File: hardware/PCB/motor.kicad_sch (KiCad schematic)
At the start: 32 parts, among them J1 Turntable Stepper, J2 Gantry Stepper, J3 Extruder Stepper, J4 Revolute Stepper

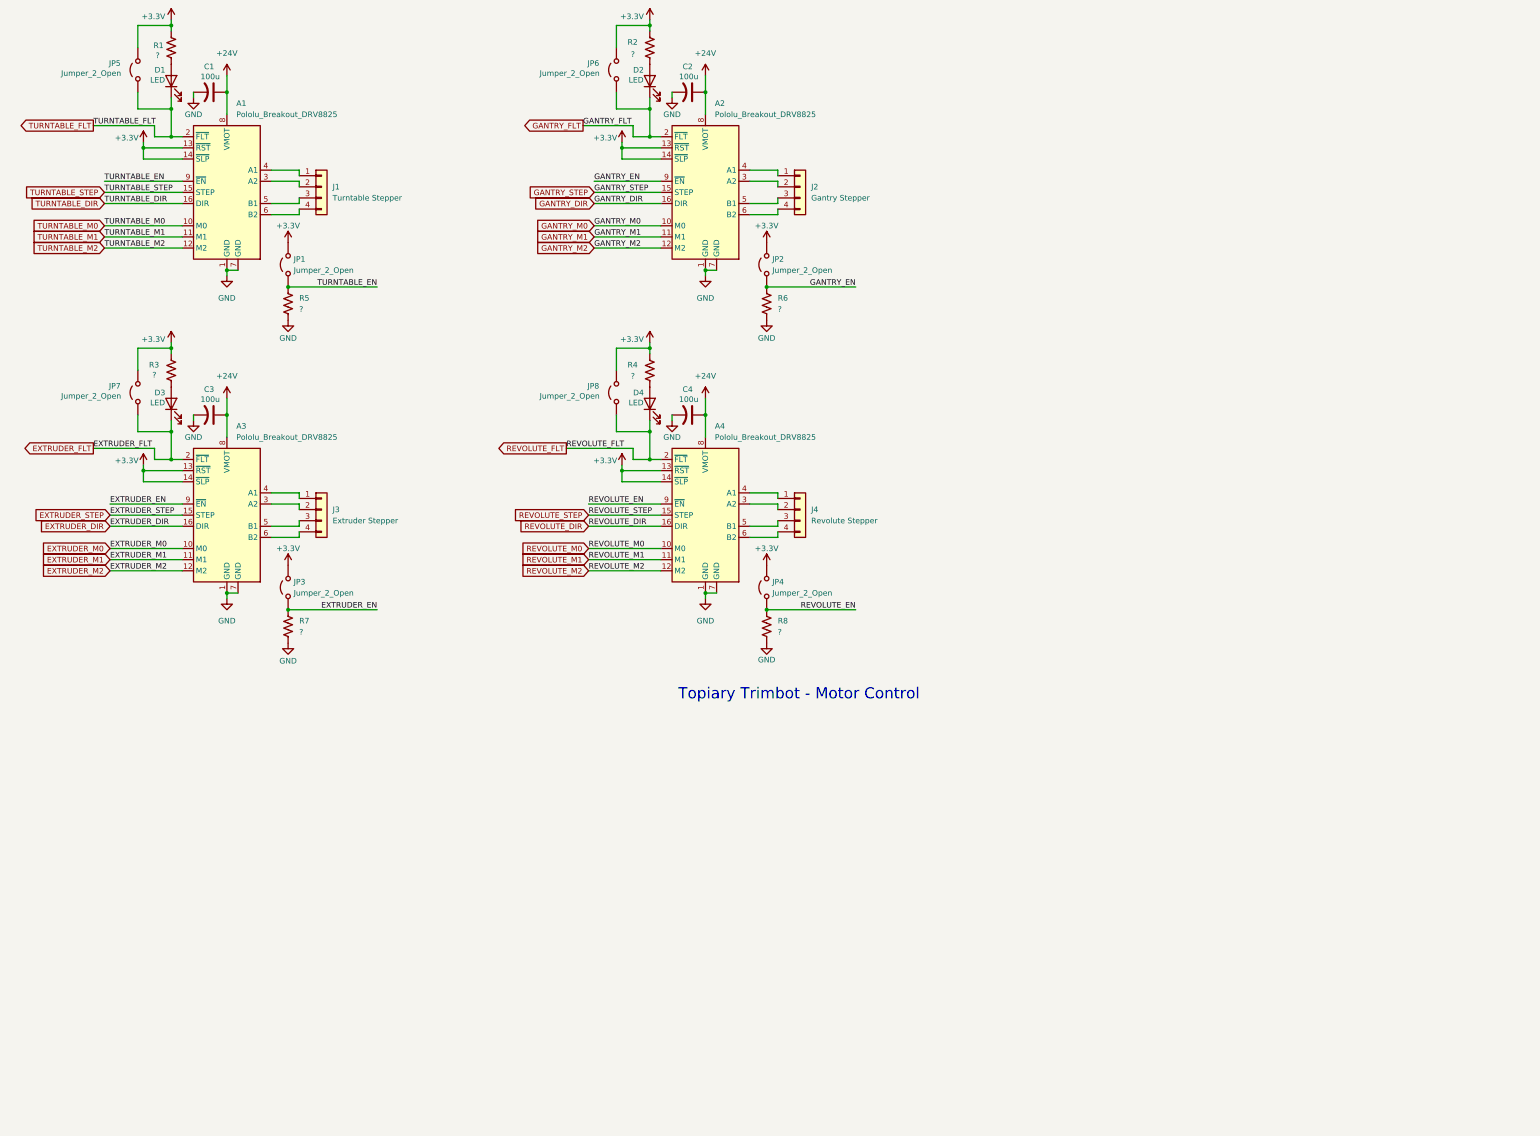
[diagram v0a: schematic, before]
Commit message: Schematic - Microstepping Jumpers
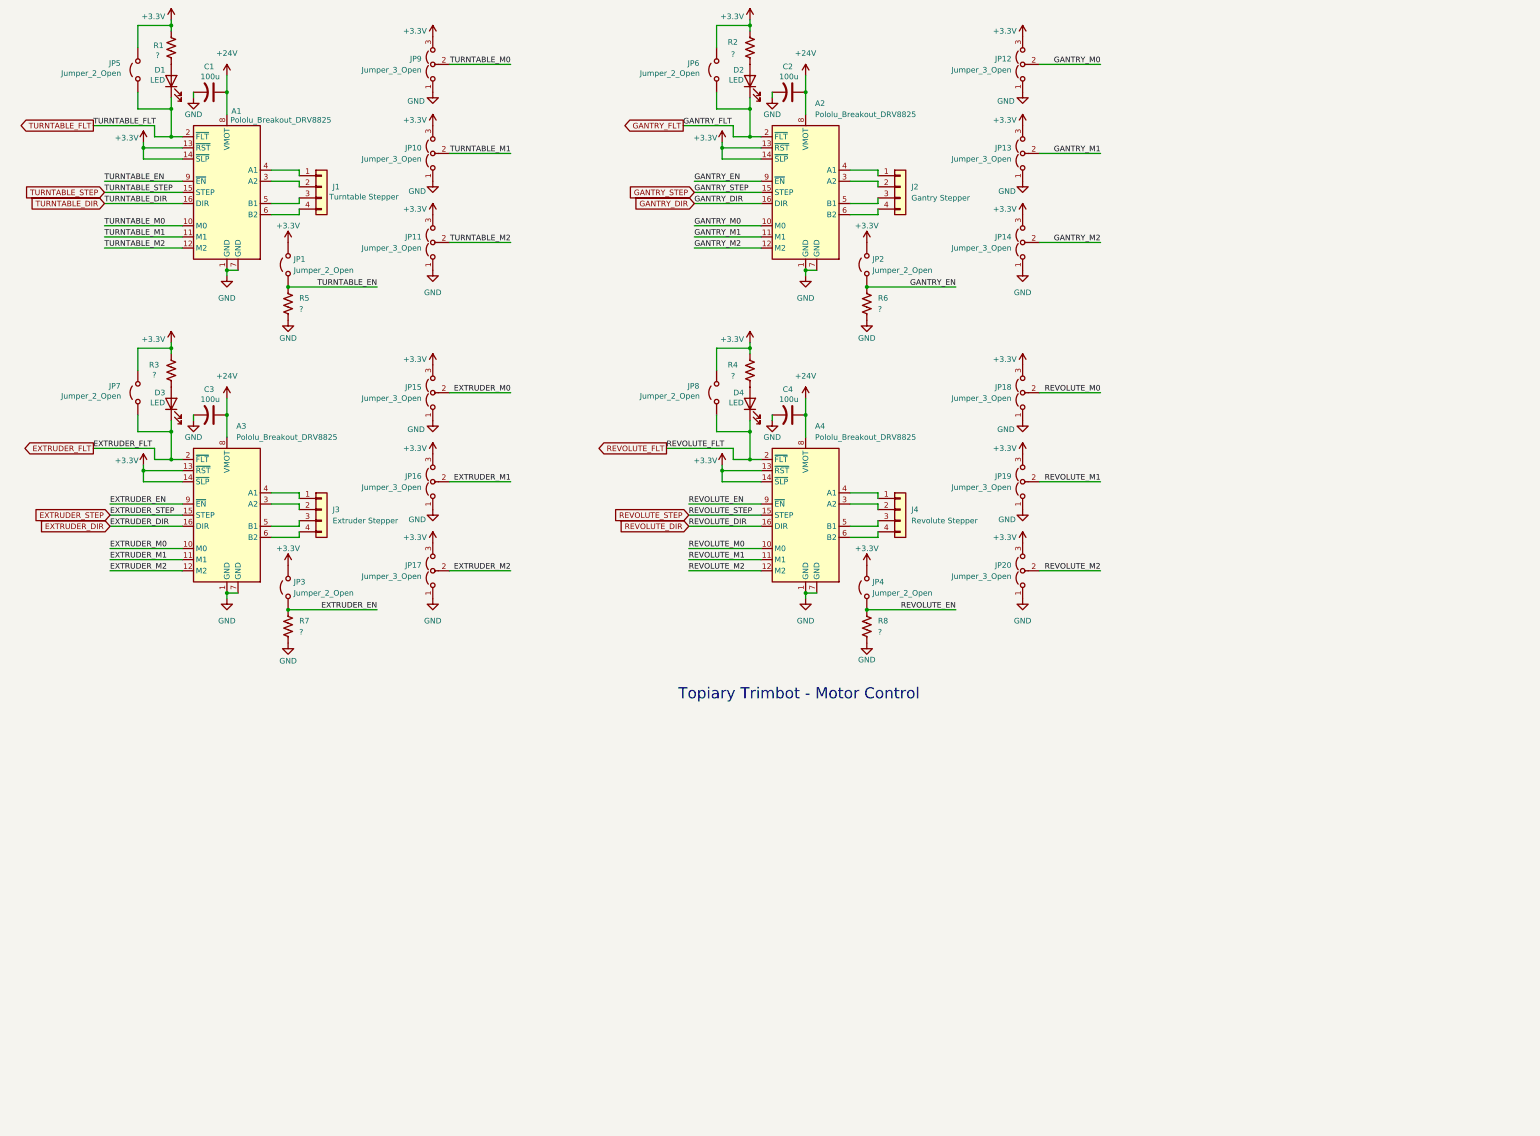
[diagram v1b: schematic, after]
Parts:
- added JP10, JP11, JP12, JP13, JP14, JP15, JP16, JP17, JP18, JP19, JP20, JP9: Jumper_3_Open, symbol Jumper:Jumper_3_Open
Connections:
- net +3.3V: now also JP10.3 (B), JP11.3 (B), JP12.3 (B), JP13.3 (B), JP14.3 (B), JP15.3 (B), JP16.3 (B), JP17.3 (B), JP18.3 (B), JP19.3 (B), JP20.3 (B), JP9.3 (B)
- net EXTRUDER_M0: now also JP15.2 (C)
- net EXTRUDER_M1: now also JP16.2 (C)
- net EXTRUDER_M2: now also JP17.2 (C)
- net GANTRY_M0: now also JP12.2 (C)
- net GANTRY_M1: now also JP13.2 (C)
- net GANTRY_M2: now also JP14.2 (C)
- net GND: now also JP10.1 (A), JP11.1 (A), JP12.1 (A), JP13.1 (A), JP14.1 (A), JP15.1 (A), JP16.1 (A), JP17.1 (A), JP18.1 (A), JP19.1 (A), JP20.1 (A), JP9.1 (A)
- net REVOLUTE_M0: now also JP18.2 (C)
- net REVOLUTE_M1: now also JP19.2 (C)
- net REVOLUTE_M2: now also JP20.2 (C)
- net TURNTABLE_M0: now also JP9.2 (C)
- net TURNTABLE_M1: now also JP10.2 (C)
- net TURNTABLE_M2: now also JP11.2 (C)
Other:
- moved on the sheet: A2, A4, C2, C4, D2, D4, J2, J4, JP2, JP4, JP6, JP8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

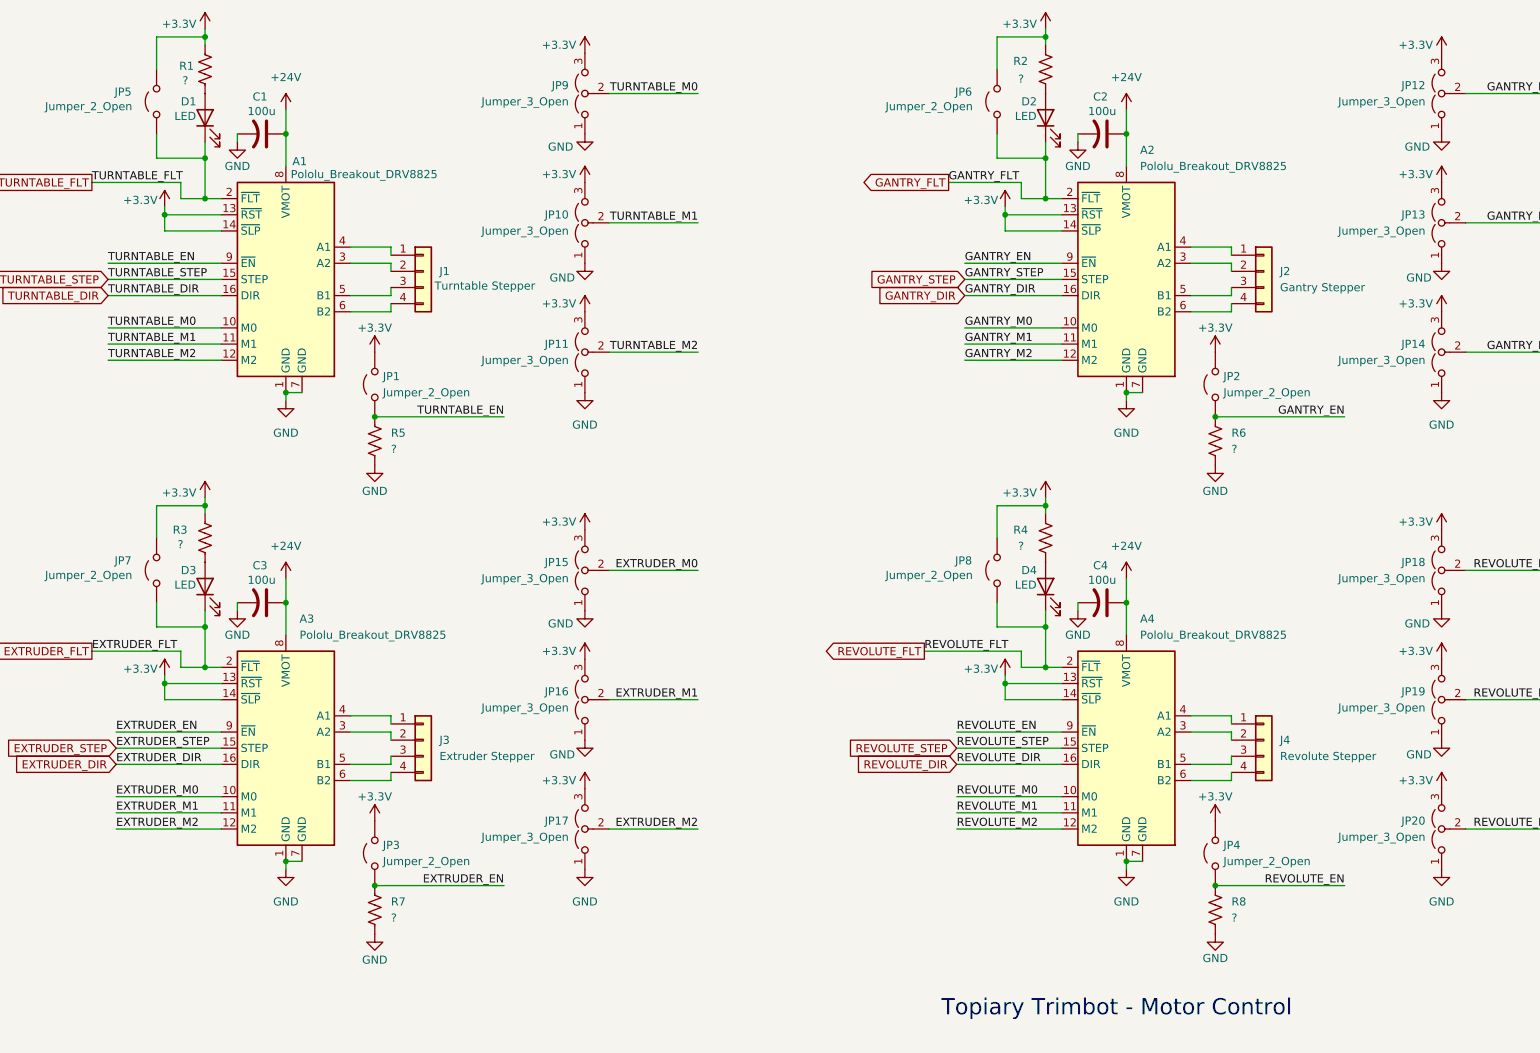
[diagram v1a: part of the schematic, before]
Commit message: Schematic: add manufacturer PN field and start picking parts and footprints in LCD and Motor
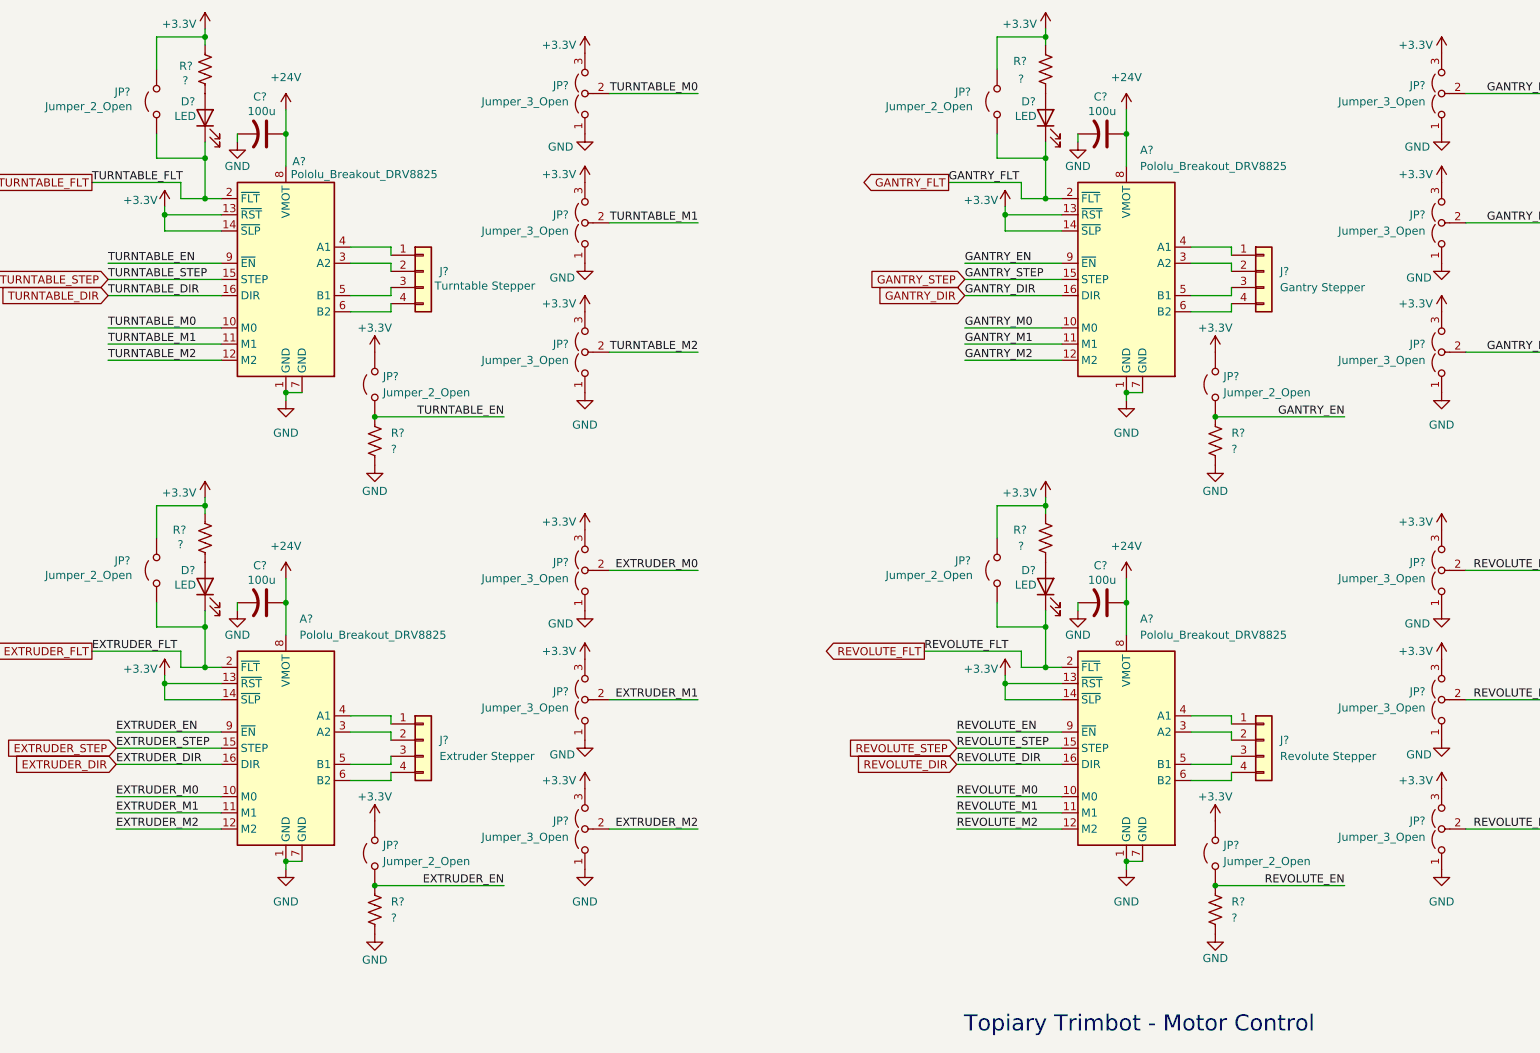
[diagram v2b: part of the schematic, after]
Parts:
- A?: renamed from A4; Manufacturer_Part_Number (none) -> DRV8825
- A?: renamed from A3; Manufacturer_Part_Number (none) -> DRV8825
- A?: renamed from A2; Manufacturer_Part_Number (none) -> DRV8825
- A?: renamed from A1; Manufacturer_Part_Number (none) -> DRV8825
- C?: renamed from C4; footprint (none) -> Capacitor_THT:C_Radial_D8.0mm_H11.5mm_P3.50mm; Manufacturer_Part_Number (none) -> UVR1H101MPD1TD
- C?: renamed from C3; footprint (none) -> Capacitor_THT:C_Radial_D8.0mm_H11.5mm_P3.50mm; Manufacturer_Part_Number (none) -> UVR1H101MPD1TD
- C?: renamed from C1; footprint (none) -> Capacitor_THT:C_Radial_D8.0mm_H11.5mm_P3.50mm; Manufacturer_Part_Number (none) -> UVR1H101MPD1TD
- C?: renamed from C2; footprint (none) -> Capacitor_THT:C_Radial_D8.0mm_H11.5mm_P3.50mm; Manufacturer_Part_Number (none) -> UVR1H101MPD1TD
- J?: renamed from J4; Manufacturer_Part_Number (none) -> 0022232041
- J?: renamed from J1; Manufacturer_Part_Number (none) -> 0022232041
- J?: renamed from J2; Manufacturer_Part_Number (none) -> 0022232041
- J?: renamed from J3; Manufacturer_Part_Number (none) -> 0022232041
- JP?: renamed from JP18; footprint (none) -> Connector_PinHeader_1.00mm:PinHeader_1x03_P1.00mm_Vertical
- JP?: renamed from JP10; footprint (none) -> Connector_PinHeader_1.00mm:PinHeader_1x03_P1.00mm_Vertical
- JP?: renamed from JP7; footprint (none) -> Connector_PinHeader_1.00mm:PinHeader_1x02_P1.00mm_Vertical
- JP?: renamed from JP11; footprint (none) -> Connector_PinHeader_1.00mm:PinHeader_1x03_P1.00mm_Vertical
- JP?: renamed from JP2; footprint (none) -> Connector_PinHeader_1.00mm:PinHeader_1x02_P1.00mm_Vertical
- JP?: renamed from JP14; footprint (none) -> Connector_PinHeader_1.00mm:PinHeader_1x03_P1.00mm_Vertical
- JP?: renamed from JP19; footprint (none) -> Connector_PinHeader_1.00mm:PinHeader_1x03_P1.00mm_Vertical
- JP?: renamed from JP15; footprint (none) -> Connector_PinHeader_1.00mm:PinHeader_1x03_P1.00mm_Vertical
- JP?: renamed from JP4; footprint (none) -> Connector_PinHeader_1.00mm:PinHeader_1x02_P1.00mm_Vertical
- JP?: renamed from JP3; footprint (none) -> Connector_PinHeader_1.00mm:PinHeader_1x02_P1.00mm_Vertical
- JP?: renamed from JP6; footprint (none) -> Connector_PinHeader_1.00mm:PinHeader_1x02_P1.00mm_Vertical
- JP?: renamed from JP13; footprint (none) -> Connector_PinHeader_1.00mm:PinHeader_1x03_P1.00mm_Vertical
- JP?: renamed from JP1; footprint (none) -> Connector_PinHeader_1.00mm:PinHeader_1x02_P1.00mm_Vertical
- JP?: renamed from JP20; footprint (none) -> Connector_PinHeader_1.00mm:PinHeader_1x03_P1.00mm_Vertical
- JP?: renamed from JP17; footprint (none) -> Connector_PinHeader_1.00mm:PinHeader_1x03_P1.00mm_Vertical
- JP?: renamed from JP8; footprint (none) -> Connector_PinHeader_1.00mm:PinHeader_1x02_P1.00mm_Vertical
- JP?: renamed from JP16; footprint (none) -> Connector_PinHeader_1.00mm:PinHeader_1x03_P1.00mm_Vertical
- JP?: renamed from JP12; footprint (none) -> Connector_PinHeader_1.00mm:PinHeader_1x03_P1.00mm_Vertical
- JP?: renamed from JP9; footprint (none) -> Connector_PinHeader_1.00mm:PinHeader_1x03_P1.00mm_Vertical
- JP?: renamed from JP5; footprint (none) -> Connector_PinHeader_1.00mm:PinHeader_1x02_P1.00mm_Vertical
- R?: renamed from R7; footprint (none) -> Resistor_SMD:R_0805_2012Metric
- R?: renamed from R3; footprint (none) -> Resistor_SMD:R_0805_2012Metric
- R?: renamed from R5; footprint (none) -> Resistor_SMD:R_0805_2012Metric
- R?: renamed from R1; footprint (none) -> Resistor_SMD:R_0805_2012Metric
- R?: renamed from R4; footprint (none) -> Resistor_SMD:R_0805_2012Metric
- R?: renamed from R2; footprint (none) -> Resistor_SMD:R_0805_2012Metric
- R?: renamed from R6; footprint (none) -> Resistor_SMD:R_0805_2012Metric
- R?: renamed from R8; footprint (none) -> Resistor_SMD:R_0805_2012Metric
- renumbered D2 to D?, D3 to D?, D4 to D?, D1 to D?
